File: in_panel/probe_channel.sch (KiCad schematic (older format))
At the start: 1 part, among them J201 Input card

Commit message: More work on in_panel.  Also, shortened input_board by 10mm and tweaked the testpoints a bit, added another GND, and changed the supply TPs to be a hookable type.
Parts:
- J201: footprint Connector_RJ:RJ45_Amphenol_RJHSE538X -> input:RJ45_Amphenol_RJHSE5380; DK line 18 -> (none); Description CONN MOD JACK 8P8C R/A SHIELDED -> (none); Digikey RJHSE5387-ND -> (none); MPN RJHSE5387 -> (none)
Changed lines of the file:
@@
 $Descr A4 11693 8268
 encoding utf-8
-Sheet 12 16
+Sheet 2 16
 Title ""
 Date ""
@@
 AR Path="/60030EBA/60020BBA" Ref="J701"  Part="1"
 AR Path="/60030EFF/60020BBA" Ref="J1201"  Part="1"
-F 0 "J1201" H 6700 3300 50  0000 R CNN
+F 0 "J201" H 6700 3300 50  0000 R CNN
 F 1 "Input card" H 6800 3300 50  0000 L CNN
-F 2 "Connector_RJ:RJ45_Amphenol_RJHSE538X" V 6900 2775 50  0001 C CNN
-F 3 "https://cdn.amphenol-icc.com/media/wysiwyg/files/drawing/rjhse538x.pdf" V 6900 2775 50  0001 C CNN
-F 4 "RJHSE5387-ND" H 6900 2750 50  0001 C CNN "Digikey"
-F 5 "RJHSE5387" H 6900 2750 50  0001 C CNN "MPN"
-F 6 "CONN MOD JACK 8P8C R/A SHIELDED" H 6900 2750 50  0001 C CNN "Description"
-F 7 "18" H 6900 2750 50  0001 C CNN "DK line"
+F 2 "input:RJ45_Amphenol_RJHSE5380" V 6900 2775 50  0001 C CNN
+F 3 "?" V 6900 2775 50  0001 C CNN
+F 4 "" H 6900 2750 50  0001 C CNN "Digikey"
+F 5 "" H 6900 2750 50  0001 C CNN "MPN"
+F 6 "" H 6900 2750 50  0001 C CNN "Description"
+F 7 "" H 6900 2750 50  0001 C CNN "DK line"
 F 8 "Amphenol ICC (Commercial Products)" H 6900 2750 50  0001 C CNN "Manufacturer"
 	1    6900 2750
@@
 AR Path="/60030EBA/60020BCE" Ref="#PWR0701"  Part="1"
 AR Path="/60030EFF/60020BCE" Ref="#PWR01201"  Part="1"
-F 0 "#PWR01201" H 6900 3150 50  0001 C CNN
+F 0 "#PWR0201" H 6900 3150 50  0001 C CNN
 F 1 "Earth" H 6900 3250 50  0001 C CNN
 F 2 "" H 6900 3400 50  0001 C CNN

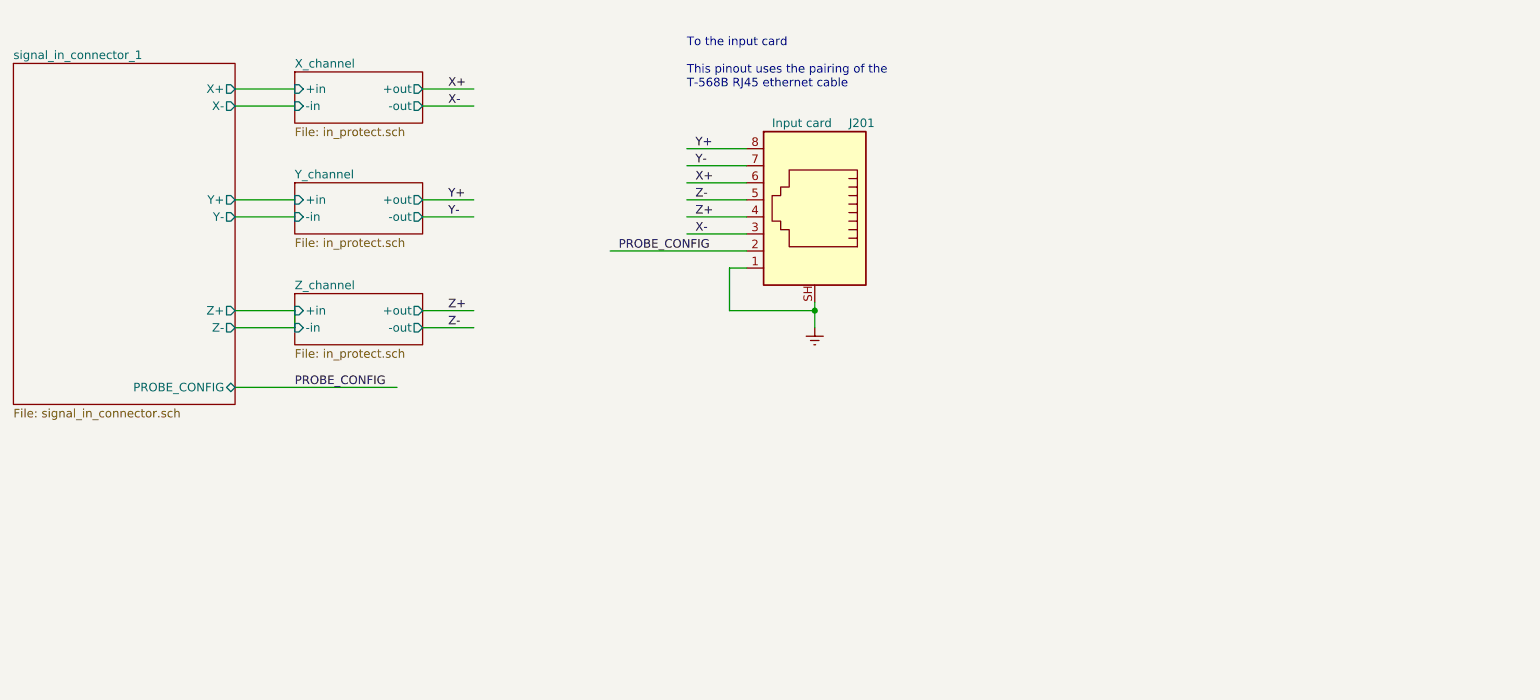
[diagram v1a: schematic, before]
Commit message: in_panel is nearly complete, input/adc.sch: change testpoint style to loop. input/input_channel.sch: modification seems spurious
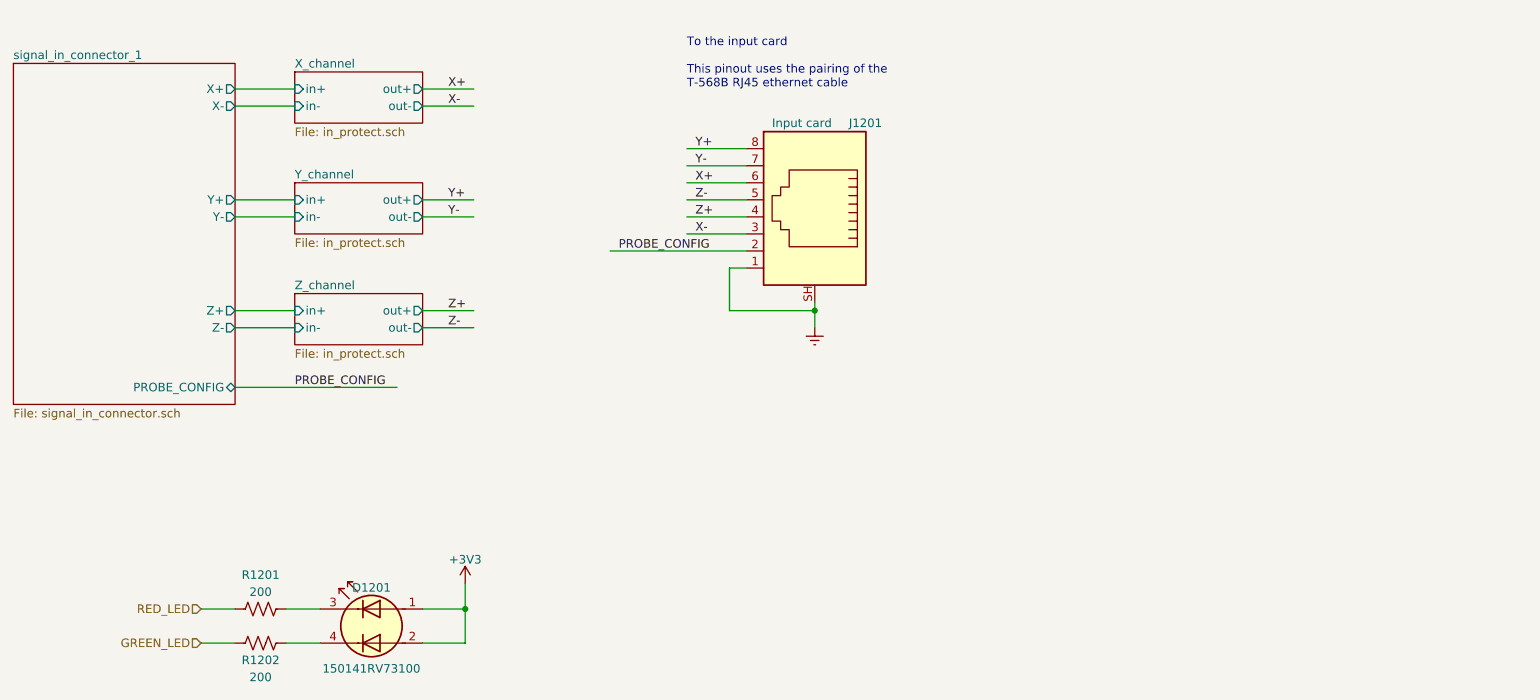
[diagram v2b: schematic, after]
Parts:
- added D201: 150141RV73100, input:LED_Wurth-PLCC4_3.2x2.8mm, symbol Device:LED_Dual_AACC
- added R201, R202: 200, Resistor_SMD:R_0603_1608Metric, symbol Device:R_US
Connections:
- net labels added: +3V3, GREEN_LED, RED_LED
- wire segments 26 -> 33
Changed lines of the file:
@@
 $Descr A4 11693 8268
 encoding utf-8
-Sheet 2 16
+Sheet 12 16
 Title ""
 Date ""
@@
 F0 "X_channel" 50
 F1 "in_protect.sch" 50
-F2 "-in" I L 3850 2100 50
-F3 "+in" I L 3850 2000 50
-F4 "+out" O R 4600 2000 50
-F5 "-out" O R 4600 2100 50
+F2 "in-" I L 3850 2100 50
+F3 "in+" I L 3850 2000 50
+F4 "out+" O R 4600 2000 50
+F5 "out-" O R 4600 2100 50
 $EndSheet
 $Sheet
@@
 F0 "Y_channel" 50
 F1 "in_protect.sch" 50
-F2 "-in" I L 3850 2750 50
-F3 "+in" I L 3850 2650 50
-F4 "+out" O R 4600 2650 50
-F5 "-out" O R 4600 2750 50
+F2 "in-" I L 3850 2750 50
+F3 "in+" I L 3850 2650 50
+F4 "out+" O R 4600 2650 50
+F5 "out-" O R 4600 2750 50
 $EndSheet
 $Sheet
@@
 F0 "Z_channel" 50
 F1 "in_protect.sch" 50
-F2 "-in" I L 3850 3400 50
-F3 "+in" I L 3850 3300 50
-F4 "+out" O R 4600 3300 50
-F5 "-out" O R 4600 3400 50
+F2 "in-" I L 3850 3400 50
+F3 "in+" I L 3850 3300 50
+F4 "out+" O R 4600 3300 50
+F5 "out-" O R 4600 3400 50
 $EndSheet
 Wire Wire Line
@@
 AR Path="/60030EBA/60020BBA" Ref="J701"  Part="1"
 AR Path="/60030EFF/60020BBA" Ref="J1201"  Part="1"
-F 0 "J201" H 6700 3300 50  0000 R CNN
+F 0 "J1201" H 6700 3300 50  0000 R CNN
 F 1 "Input card" H 6800 3300 50  0000 L CNN
 F 2 "input:RJ45_Amphenol_RJHSE5380" V 6900 2775 50  0001 C CNN
@@
 AR Path="/60030EBA/60020BCE" Ref="#PWR0701"  Part="1"
 AR Path="/60030EFF/60020BCE" Ref="#PWR01201"  Part="1"
-F 0 "#PWR0201" H 6900 3150 50  0001 C CNN
+F 0 "#PWR01201" H 6900 3150 50  0001 C CNN
 F 1 "Earth" H 6900 3250 50  0001 C CNN
 F 2 "" H 6900 3400 50  0001 C CNN
@@
 	3850 2750 3500 2750
 Wire Wire Line
-	3850 3300 3850 3400
-Wire Wire Line
 	3850 3400 3500 3400
 Wire Wire Line
 	3850 3300 3500 3300
+$Comp
+L Device:LED_Dual_AACC D201
+U 1 1 600CE01A
+P 4300 5150
+AR Path="/600141C9/600CE01A" Ref="D201"  Part="1"
+AR Path="/60030EBA/600CE01A" Ref="D701"  Part="1"
+AR Path="/60030EFF/600CE01A" Ref="D1201"  Part="1"
+F 0 "D1201" H 4300 5375 50  0000 C CNN
+F 1 "150141RV73100" H 4300 4900 50  0000 C CNN
+F 2 "input:LED_Wurth-PLCC4_3.2x2.8mm" H 4330 5150 50  0001 C CNN
+F 3 "~" H 4330 5150 50  0001 C CNN
+	1    4300 5150
+	-1   0    0    -1
+$EndComp
+$Comp
+L power:+3V3 #PWR0107
+U 1 1 600D16FB
+P 4850 4900
+AR Path="/600141C9/600D16FB" Ref="#PWR0107"  Part="1"
+AR Path="/60030EBA/600D16FB" Ref="#PWR0108"  Part="1"
+AR Path="/60030EFF/600D16FB" Ref="#PWR0109"  Part="1"
+F 0 "#PWR0109" H 4850 4750 50  0001 C CNN
+F 1 "+3V3" H 4850 5040 50  0000 C CNN
+F 2 "" H 4850 4900 50  0001 C CNN
+F 3 "" H 4850 4900 50  0001 C CNN
+	1    4850 4900
+	1    0    0    -1
+$EndComp
+$Comp
+L Device:R_US R201
+U 1 1 600D2722
+P 3650 5050
+AR Path="/600141C9/600D2722" Ref="R201"  Part="1"
+AR Path="/60030EBA/600D2722" Ref="R701"  Part="1"
+AR Path="/60030EFF/600D2722" Ref="R1201"  Part="1"
+F 0 "R1201" V 3450 5050 50  0000 C CNN
+F 1 "200" V 3550 5050 50  0000 C CNN
+F 2 "Resistor_SMD:R_0603_1608Metric" V 3690 5040 50  0001 C CNN
+F 3 "~" H 3650 5050 50  0001 C CNN
+	1    3650 5050
+	0    1    1    0
+$EndComp
+$Comp
+L Device:R_US R202
+U 1 1 600D2E7B
+P 3650 5250
+AR Path="/600141C9/600D2E7B" Ref="R202"  Part="1"
+AR Path="/60030EBA/600D2E7B" Ref="R702"  Part="1"
+AR Path="/60030EFF/600D2E7B" Ref="R1202"  Part="1"
+F 0 "R1202" V 3750 5250 50  0000 C CNN
+F 1 "200" V 3850 5250 50  0000 C CNN
+F 2 "Resistor_SMD:R_0603_1608Metric" V 3690 5240 50  0001 C CNN
+F 3 "~" H 3650 5250 50  0001 C CNN
+	1    3650 5250
+	0    1    1    0
+$EndComp
+Wire Wire Line
+	4600 5050 4850 5050
+Wire Wire Line
+	4850 5050 4850 4900
+Wire Wire Line
+	4600 5250 4850 5250
+Wire Wire Line
+	4850 5250 4850 5050
+Connection ~ 4850 5050
+Text HLabel 3300 5050 0    50   Input ~ 0
+RED_LED
+Text HLabel 3300 5250 0    50   Input ~ 0
+GREEN_LED
+Wire Wire Line
+	3300 5050 3500 5050
+Wire Wire Line
+	3300 5250 3500 5250
+Wire Wire Line
+	3800 5050 4000 5050
+Wire Wire Line
+	3800 5250 4000 5250
 $EndSCHEMATC

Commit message: Revision 0 of in_panel, off to fab
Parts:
- D201: DK line (none) -> IP.3; Description (none) -> LED GREEN/RED CLEAR 3528 SMD; Digikey (none) -> 732-5001-1-ND; MPN (none) -> 150141RV73100; Manufacturer (none) -> Würth Elektronik
- J201: footprint input:RJ45_Amphenol_RJHSE5380 -> input:RJ45_Amphenol_RJHSE-338x; DK line (none) -> IP.5; Description (none) -> CONN MOD JACK 8P8C VERT SHIELDED; Digikey (none) -> RJHSE-3380-ND; MPN (none) -> RJHSE-3380
- R201, R202: DK line (none) -> I.55; Description (none) -> RES 200 OHM 1% 1/8W 0603; Digikey (none) -> RNCP0603FTD200RCT-ND; MPN (none) -> RNCP0603FTD200R; Manufacturer (none) -> Stackpole Electronics Inc
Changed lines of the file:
@@
 $Descr A4 11693 8268
 encoding utf-8
-Sheet 12 16
+Sheet 2 16
 Title ""
 Date ""
@@
 AR Path="/60030EBA/60020BBA" Ref="J701"  Part="1"
 AR Path="/60030EFF/60020BBA" Ref="J1201"  Part="1"
-F 0 "J1201" H 6700 3300 50  0000 R CNN
+F 0 "J201" H 6700 3300 50  0000 R CNN
 F 1 "Input card" H 6800 3300 50  0000 L CNN
-F 2 "input:RJ45_Amphenol_RJHSE5380" V 6900 2775 50  0001 C CNN
-F 3 "?" V 6900 2775 50  0001 C CNN
-F 4 "" H 6900 2750 50  0001 C CNN "Digikey"
-F 5 "" H 6900 2750 50  0001 C CNN "MPN"
-F 6 "" H 6900 2750 50  0001 C CNN "Description"
-F 7 "" H 6900 2750 50  0001 C CNN "DK line"
+F 2 "input:RJ45_Amphenol_RJHSE-338x" V 6900 2775 50  0001 C CNN
+F 3 "http://www.amphenol-icc.com/media/wysiwyg/files/drawing/rjhse338x.pdf" V 6900 2775 50  0001 C CNN
+F 4 "RJHSE-3380-ND" H 6900 2750 50  0001 C CNN "Digikey"
+F 5 "RJHSE-3380" H 6900 2750 50  0001 C CNN "MPN"
+F 6 "CONN MOD JACK 8P8C VERT SHIELDED" H 6900 2750 50  0001 C CNN "Description"
+F 7 "IP.5" H 6900 2750 50  0001 C CNN "DK line"
 F 8 "Amphenol ICC (Commercial Products)" H 6900 2750 50  0001 C CNN "Manufacturer"
 	1    6900 2750
@@
 AR Path="/60030EBA/60020BCE" Ref="#PWR0701"  Part="1"
 AR Path="/60030EFF/60020BCE" Ref="#PWR01201"  Part="1"
-F 0 "#PWR01201" H 6900 3150 50  0001 C CNN
+F 0 "#PWR0201" H 6900 3150 50  0001 C CNN
 F 1 "Earth" H 6900 3250 50  0001 C CNN
 F 2 "" H 6900 3400 50  0001 C CNN
@@
 AR Path="/60030EBA/600CE01A" Ref="D701"  Part="1"
 AR Path="/60030EFF/600CE01A" Ref="D1201"  Part="1"
-F 0 "D1201" H 4300 5375 50  0000 C CNN
+F 0 "D201" H 4300 5375 50  0000 C CNN
 F 1 "150141RV73100" H 4300 4900 50  0000 C CNN
 F 2 "input:LED_Wurth-PLCC4_3.2x2.8mm" H 4330 5150 50  0001 C CNN
-F 3 "~" H 4330 5150 50  0001 C CNN
+F 3 "https://katalog.we-online.de/led/datasheet/150141RV73100.pdf" H 4330 5150 50  0001 C CNN
+F 4 "150141RV73100" H 4300 5150 50  0001 C CNN "MPN"
+F 5 "IP.3" H 4300 5150 50  0001 C CNN "DK line"
+F 6 "LED GREEN/RED CLEAR 3528 SMD" H 4300 5150 50  0001 C CNN "Description"
+F 7 "732-5001-1-ND" H 4300 5150 50  0001 C CNN "Digikey"
+F 8 "Würth Elektronik" H 4300 5150 50  0001 C CNN "Manufacturer"
 	1    4300 5150
 	-1   0    0    -1
@@
 AR Path="/60030EBA/600D16FB" Ref="#PWR0108"  Part="1"
 AR Path="/60030EFF/600D16FB" Ref="#PWR0109"  Part="1"
-F 0 "#PWR0109" H 4850 4750 50  0001 C CNN
+F 0 "#PWR0107" H 4850 4750 50  0001 C CNN
 F 1 "+3V3" H 4850 5040 50  0000 C CNN
 F 2 "" H 4850 4900 50  0001 C CNN
@@
 AR Path="/60030EBA/600D2722" Ref="R701"  Part="1"
 AR Path="/60030EFF/600D2722" Ref="R1201"  Part="1"
-F 0 "R1201" V 3450 5050 50  0000 C CNN
+F 0 "R201" V 3450 5050 50  0000 C CNN
 F 1 "200" V 3550 5050 50  0000 C CNN
 F 2 "Resistor_SMD:R_0603_1608Metric" V 3690 5040 50  0001 C CNN
 F 3 "~" H 3650 5050 50  0001 C CNN
+F 4 "I.55" H 3650 5050 50  0001 C CNN "DK line"
+F 5 "RES 200 OHM 1% 1/8W 0603" H 3650 5050 50  0001 C CNN "Description"
+F 6 "RNCP0603FTD200RCT-ND" H 3650 5050 50  0001 C CNN "Digikey"
+F 7 "RNCP0603FTD200R" H 3650 5050 50  0001 C CNN "MPN"
+F 8 "Stackpole Electronics Inc" H 3650 5050 50  0001 C CNN "Manufacturer"
 	1    3650 5050
 	0    1    1    0
@@
 AR Path="/60030EBA/600D2E7B" Ref="R702"  Part="1"
 AR Path="/60030EFF/600D2E7B" Ref="R1202"  Part="1"
-F 0 "R1202" V 3750 5250 50  0000 C CNN
+F 0 "R202" V 3750 5250 50  0000 C CNN
 F 1 "200" V 3850 5250 50  0000 C CNN
 F 2 "Resistor_SMD:R_0603_1608Metric" V 3690 5240 50  0001 C CNN
 F 3 "~" H 3650 5250 50  0001 C CNN
+F 4 "I.55" H 3650 5250 50  0001 C CNN "DK line"
+F 5 "RES 200 OHM 1% 1/8W 0603" H 3650 5250 50  0001 C CNN "Description"
+F 6 "RNCP0603FTD200RCT-ND" H 3650 5250 50  0001 C CNN "Digikey"
+F 7 "RNCP0603FTD200R" H 3650 5250 50  0001 C CNN "MPN"
+F 8 "Stackpole Electronics Inc" H 3650 5250 50  0001 C CNN "Manufacturer"
 	1    3650 5250
 	0    1    1    0

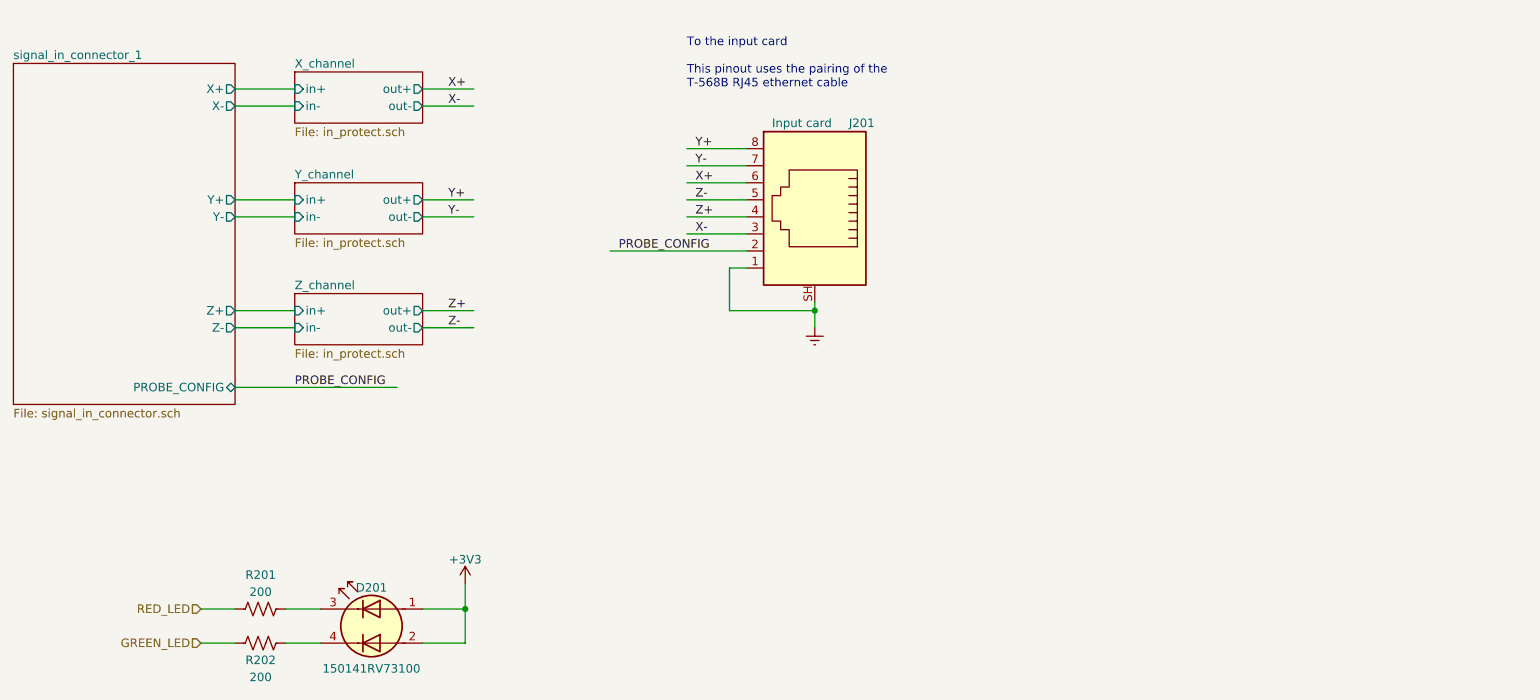
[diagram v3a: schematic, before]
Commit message: Mainly much more detailed documentation of the sensor pinout wrt the RJ45 standards, see docs/Rj45_probe_pinout.xlsx
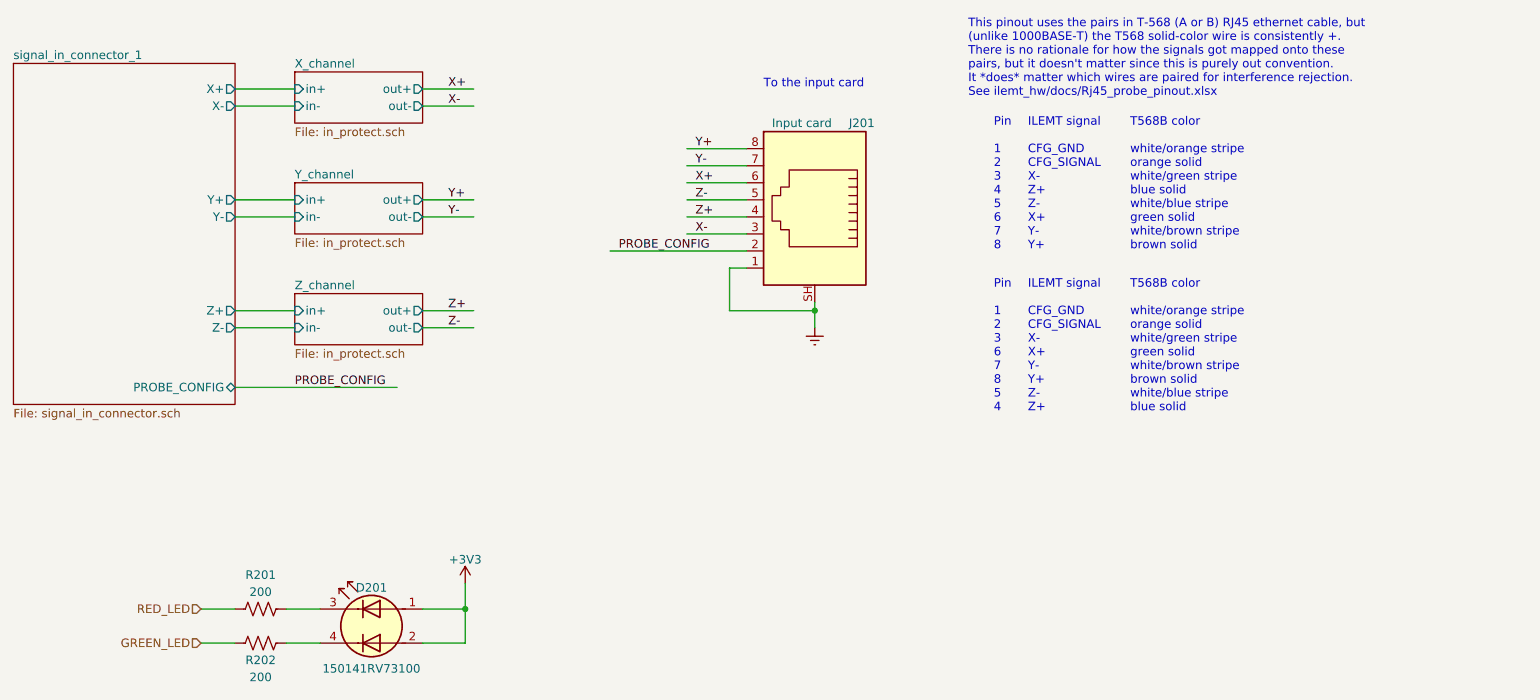
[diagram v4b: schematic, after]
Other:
- note added: "ILEMT signal\n\nCFG_GND\nCFG_SIGNAL\nX-\nX+\nY-\nY+\nZ-\nZ+\n"
- note added: "ILEMT signal\n\nCFG_GND\nCFG_SIGNAL\nX-\nZ+\nZ-\nX+\nY-\nY+\n"
- note added: "Pin\n\n1\n2\n3\n4\n5\n6\n7\n8\n"
- note added: "Pin\n\n1\n2\n3\n6\n7\n8\n5\n4"
- note added: "T568B color\n\nwhite/orange stripe\norange solid\nwhite/green stripe\nblue solid\nwhite/blue stripe\ngreen solid\nwhite/brown stripe\nbrown solid\n"
- note added: "T568B color\n\nwhite/orange stripe\norange solid\nwhite/green stripe\ngreen solid\nwhite/brown stripe\nbrown solid\nwhite/blue stripe\nblue solid"
- note added: "This pinout uses the pairs in T-568 (A or B) RJ45 ethernet cable, but\n(unlike 1000BASE-T) the T568 solid-color wire is consistently +.\nThere is no rationale for how the signals got mapped onto these\npairs, but it doesn't matter since this is purely out convention.\nIt *does* matter which wires are paired for interference rejection.\nSee ilemt_hw/docs/Rj45_probe_pinout.xlsx"
- note added: "To the input card\n"
- note removed: "To the input card\n\nThis pinout uses the pairing of the \nT-568B RJ45 ethernet cable"
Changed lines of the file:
@@
 Wire Wire Line
 	6500 2750 6150 2750
-Text Notes 6150 2000 0    50   ~ 0
-To the input card\n\nThis pinout uses the pairing of the \nT-568B RJ45 ethernet cable
+Text Notes 6600 2000 0    50   ~ 0
+To the input card\n
 $Comp
 L power:Earth #PWR?
@@
 Wire Wire Line
 	3800 5250 4000 5250
+Text Notes 7800 2050 0    50   ~ 0
+This pinout uses the pairs in T-568 (A or B) RJ45 ethernet cable, but\n(unlike 1000BASE-T) the T568 solid-color wire is consistently +.\nThere is no rationale for how the signals got mapped onto these\npairs, but it doesn't matter since this is purely out convention.\nIt *does* matter which wires are paired for interference rejection.\nSee ilemt_hw/docs/Rj45_probe_pinout.xlsx
+Text Notes 8150 2950 0    50   ~ 0
+ILEMT signal\n\nCFG_GND\nCFG_SIGNAL\nX-\nZ+\nZ-\nX+\nY-\nY+\n
+Text Notes 7950 2950 0    50   ~ 0
+Pin\n\n1\n2\n3\n4\n5\n6\n7\n8\n
+Text Notes 8750 2950 0    50   ~ 0
+T568B color\n\nwhite/orange stripe\norange solid\nwhite/green stripe\nblue solid\nwhite/blue stripe\ngreen solid\nwhite/brown stripe\nbrown solid\n
+Text Notes 8150 3900 0    50   ~ 0
+ILEMT signal\n\nCFG_GND\nCFG_SIGNAL\nX-\nX+\nY-\nY+\nZ-\nZ+\n
+Text Notes 8750 3900 0    50   ~ 0
+T568B color\n\nwhite/orange stripe\norange solid\nwhite/green stripe\ngreen solid\nwhite/brown stripe\nbrown solid\nwhite/blue stripe\nblue solid
+Text Notes 7950 3900 0    50   ~ 0
+Pin\n\n1\n2\n3\n6\n7\n8\n5\n4
 $EndSCHEMATC
